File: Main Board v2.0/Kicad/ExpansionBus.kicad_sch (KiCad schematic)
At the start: 0 parts

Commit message: update
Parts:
- added C24, C25, C26, C27, C28: 100n, symbol Device:C
- added J1: Bus_ISA_16bit, Connector_PCBEdge:BUS_AT, symbol Connector:Bus_ISA_16bit
- added U13, U14, U15: 74HC245, symbol 74xx:74HC245
- added U17, U18: 74HC646, symbol My-74-Logic:74HC646
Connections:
- new net +12V: J1.9 (+12V)
- new net +5V: C24.1, C25.1, C26.1, C27.1, C28.1, J1.29 (VCC), J1.3 (+5V), J1.78 (+5V), U13.20 (VCC), U14.20 (VCC), U15.20 (VCC), U17.24 (VCC), U18.24 (VCC)
- new net -12V: J1.7 (-12V)
- new net -5V: J1.5 (-5V)
- new net A0: U13.2 (A0)
- new net A1: U13.3 (A1)
- new net A10: U14.4 (A2)
- new net A11: U14.5 (A3)
- new net A12: U14.6 (A4)
- new net A2: U13.4 (A2)
- new net A3: U13.5 (A3)
- new net A4: U13.6 (A4)
- new net A5: U13.7 (A5)
- new net A6: U13.8 (A6)
- new net A7: U13.9 (A7)
- new net A8: U14.2 (A0)
- new net A9: U14.3 (A1)
- new net BA0: J1.62 (BA00), U13.18 (B0)
- new net BA1: J1.61 (BA01), U13.17 (B1)
- new net BA10: J1.52 (BA10), U14.16 (B2)
- new net BA11: J1.51 (BA11), U14.15 (B3)
- new net BA12: J1.50 (BA12), U14.14 (B4)
- new net BA13: J1.49 (BA13), U14.13 (B5)
- new net BA14: J1.48 (BA14), U14.12 (B6)
- new net BA15: J1.47 (BA15), U14.11 (B7)
- new net BA16: J1.46 (BA16), U15.18 (B0)
- new net BA17: J1.45 (BA17), J1.88 (LA17), U15.17 (B1)
- new net BA18: J1.44 (BA18), J1.87 (LA18), U15.16 (B2)
- new net BA19: J1.43 (BA19), J1.86 (LA19), U15.15 (B3)
- new net BA2: J1.60 (BA02), U13.16 (B2)
- new net BA3: J1.59 (BA03), U13.15 (B3)
- new net BA4: J1.58 (BA04), U13.14 (B4)
- new net BA5: J1.57 (BA05), U13.13 (B5)
- new net BA6: J1.56 (BA06), U13.12 (B6)
- new net BA7: J1.55 (BA07), U13.11 (B7)
- new net BA8: J1.54 (BA08), U14.18 (B0)
- new net BA9: J1.53 (BA09), U14.17 (B1)
- new net BAEN: J1.42 (AEN)
- new net BALE: J1.28 (ALE)
- new net BA_CE: U13.19 (CE), U14.19 (CE), U15.19 (CE)
- new net BA_DIR: U13.1 (A->B), U14.1 (A->B), U15.1 (A->B)
- new net BBUS_REQ: J1.79 (MASTER)
- new net BCLK: J1.20 (CLK)
- new net BD0: J1.40 (DB0), U18.20 (B0)
- new net BD1: J1.39 (DB1), U18.19 (B1)
- new net BD10: J1.93 (D10), U17.18 (B2)
- new net BD11: J1.94 (D11), U17.17 (B3)
- new net BD12: J1.95 (D12), U17.16 (B4)
- new net BD13: J1.96 (D13), U17.15 (B5)
- new net BD14: J1.97 (D14), U17.14 (B6)
- new net BD15: J1.98 (D15), U17.13 (B7)
- new net BD2: J1.38 (DB2), U18.18 (B2)
- new net BD3: J1.37 (DB3), U18.17 (B3)
- new net BD4: J1.36 (DB4), U18.16 (B4)
- new net BD5: J1.35 (DB5), U18.15 (B5)
- new net BD6: J1.34 (DB6), U18.14 (B6)
- new net BD7: J1.33 (DB7), U18.13 (B7)
- new net BD8: J1.91 (D8), U17.20 (B0)
- new net BD8_D16: J1.81 (SBHE)
- new net BD9: J1.92 (D9), U17.19 (B1)
- new net BDMA_END: J1.27 (TC)
- new net BD_DIR: U17.3 (DIR), U18.3 (DIR)
- new net BIO: J1.32 (IO)
- new net BIO_RDY: J1.41 (IO_READY)
- new net BIRQ10: J1.65 (IRQ10)
- new net BIRQ11: J1.66 (IRQ11)
- new net BIRQ12: J1.67 (IRQ12)
- new net BIRQ14: J1.69 (IRQ14)
- new net BIRQ15: J1.68 (IRQ15)
- new net BIRQ2: J1.4 (IRQ2)
- new net BIRQ3: J1.25 (IRQ3)
- new net BIRQ4: J1.24 (IRQ4)
- new net BIRQ5: J1.23 (IRQ5)
- new net BIRQ6: J1.22 (IRQ6)
- new net BIRQ7: J1.21 (IRQ7)
- new net BLA20: J1.85 (LA20), U15.14 (B4)
- new net BLA21: J1.84 (LA21), U15.13 (B5)
- new net BLA22: J1.83 (LA22), U15.12 (B6)
- new net BLA23: J1.82 (LA23), U15.11 (B7)
- new net CLK20: J1.30 (OSC)
- new net D0: U17.4 (A0), U18.4 (A0)
- new net D1: U17.5 (A1), U18.5 (A1)
- new net D2: U17.6 (A2), U18.6 (A2)
- new net D3: U17.7 (A3), U18.7 (A3)
- new net D4: U17.8 (A4), U18.8 (A4)
- new net D5: U17.9 (A5), U18.9 (A5)
- new net D6: U17.10 (A6), U18.10 (A6)
- new net D7: U17.11 (A7), U18.11 (A7)
- new net GND: C24.2, C25.2, C26.2, C27.2, C28.2, J1.1 (GND), J1.10 (GND), J1.31 (GND), J1.80 (GND), U13.10 (GND), U14.10 (GND), U15.10 (GND), U17.12 (GND), U18.12 (GND)
- new net MA13: U14.7 (A5)
- new net MA14: U14.8 (A6)
- new net MA15: U14.9 (A7)
- new net MA16: U15.2 (A0)
- new net MA17: U15.3 (A1)
- new net MA18: U15.4 (A2)
- new net MA19: U15.5 (A3)
- new net MA20: U15.6 (A4)
- new net MA21: U15.7 (A5)
- new net MA22: U15.8 (A6)
- new net MA23: U15.9 (A7)
- new net RESET: J1.2 (RESET)
- new net what?: J1.8 (UNUSED)
- new net ~{B16_IO_CS}: J1.64 (~{IOCS16})
- new net ~{B16_MEM_CS}: J1.63 (~{MEMCS16})
- new net ~{B16_MEM_RD}: J1.89 (~{MEMR})
- new net ~{B16_MEM_WR}: J1.90 (~{MEMW})
- new net ~{B8_MEM_RD}: J1.12 (~{SMEMR})
- new net ~{B8_MEM_WR}: J1.11 (~{SMEMW})
- new net ~{BIO_RD}: J1.14 (~{IOR})
- new net ~{BIO_WR}: J1.13 (~{IOW})
- new net ~{RFSH}: J1.19 (~{REFRESH})
- no-connect marks 0 -> 1
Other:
- note added: "DMA is implemented in the DMA module (ISA card)."
- title: (none) -> Expansion Bus (ISA16)

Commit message: schematic done*
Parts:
- removed C24, C25, C26, C27, C28: 100n, symbol Device:C
- removed U13, U14, U15: 74HC245, symbol 74xx:74HC245
- removed U17, U18: 74HC646, symbol My-74-Logic:74HC646
- added J2: Unused Bus Signals, Connector_PinSocket_2.54mm:PinSocket_2x20_P2.54mm_Vertical, symbol Connector_Generic:Conn_02x20_Row_Letter_First
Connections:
- net BA0 is gone; now on net A0: J1.62 (BA00)
- net BA10 is gone; now on net A10: J1.52 (BA10)
- net BA11 is gone; now on net A11: J1.51 (BA11)
- net BA12 is gone; now on net A12: J1.50 (BA12)
- net BA13 is gone; now on net MA13: J1.49 (BA13)
- net BA14 is gone; now on net MA14: J1.48 (BA14)
- net BA15 is gone; now on net MA15: J1.47 (BA15)
- net BA16 is gone; now on net MA16: J1.46 (BA16)
- net BA2 is gone; now on net A2: J1.60 (BA02)
- net BA3 is gone; now on net A3: J1.59 (BA03)
- net BA4 is gone; now on net A4: J1.58 (BA04)
- net BA5 is gone; now on net A5: J1.57 (BA05)
- net BA6 is gone; now on net A6: J1.56 (BA06)
- net BA7 is gone; now on net A7: J1.55 (BA07)
- net BA8 is gone; now on net A8: J1.54 (BA08)
- net BA9 is gone; now on net A9: J1.53 (BA09)
- net BD0 is gone; now on net D0: J1.40 (DB0)
- net BD1 is gone; now on net D1: J1.39 (DB1)
- net BD2 is gone; now on net D2: J1.38 (DB2)
- net BIO is gone; now on net BA1: J1.32 (IO)
- net BIRQ10 is gone; now on net BD3: J1.65 (IRQ10)
- net BIRQ11 is gone; now on net BD4: J1.66 (IRQ11)
- net BIRQ12 is gone; now on net BD5: J1.67 (IRQ12)
- net BIRQ14 is gone; now on net BD7: J1.69 (IRQ14)
- net BIRQ15 is gone; now on net BD6: J1.68 (IRQ15)
- net BLA20 is gone; now on net MA20: J1.85 (LA20)
- net BLA21 is gone; now on net MA21: J1.84 (LA21)
- net BLA22 is gone; now on net MA22: J1.83 (LA22)
- net BLA23 is gone; now on net MA23: J1.82 (LA23)
- net +5V: now also J2.a19 (Pin_a19)
- net A1: now also J1.61 (BA01)
- net BA1: now also J2.a1 (Pin_a1); no longer J1.61 (BA01)
- net BD10: now also J1.72 (~{DACK5}), J2.b14 (Pin_b14); no longer J1.93 (D10)
- net BD11: now also J1.73 (DRQ5), J2.b15 (Pin_b15); no longer J1.94 (D11)
- net BD12: now also J1.74 (~{DACK6}), J2.b16 (Pin_b16); no longer J1.95 (D12)
- net BD13: now also J1.75 (DRQ6), J2.b17 (Pin_b17); no longer J1.96 (D13)
- net BD14: now also J1.76 (~{DACK7}), J2.b18 (Pin_b18); no longer J1.97 (D14)
- net BD15: now also J1.77 (DRQ7), J2.b19 (Pin_b19); no longer J1.98 (D15)
- net BD3: now also J2.b7 (Pin_b7); no longer J1.37 (DB3)
- net BD4: now also J2.b8 (Pin_b8); no longer J1.36 (DB4)
- net BD5: now also J2.b9 (Pin_b9); no longer J1.35 (DB5)
- net BD6: now also J2.b10 (Pin_b10); no longer J1.34 (DB6)
- net BD7: now also J2.b11 (Pin_b11); no longer J1.33 (DB7)
- net BD8: now also J1.70 (~{DACK0}), J2.b12 (Pin_b12); no longer J1.91 (D8)
- net BD9: now also J1.71 (DRQ0), J2.b13 (Pin_b13); no longer J1.92 (D9)
- net D3: now also J1.37 (DB3)
- net D4: now also J1.36 (DB4)
- net D5: now also J1.35 (DB5)
- net D6: now also J1.34 (DB6)
- net D7: now also J1.33 (DB7)
- net GND: now also J2.a18 (Pin_a18), J2.a20 (Pin_a20)
- net MA17: now also J1.45 (BA17)
- net MA18: now also J1.44 (BA18)
- net MA19: now also J1.43 (BA19)
- net MA24: now also J1.88 (LA17)
- net MA25: now also J1.87 (LA18)
- net BB15: now reaches J1.15 (~{DACK3})
- net BB15: now also J2.b2 (Pin_b2)
- net BB16: now reaches J1.16 (DRQ3)
- net BB16: now also J2.b3 (Pin_b3)
- net ~{CPU_BUSACK}: now reaches J1.17 (~{DACK1})
- net ~{CPU_BUSRQ}: now reaches J1.18 (DRQ1)
- net BB26: now reaches J1.26 (~{DACK2})
- net BB26: now also J2.b4 (Pin_b4)
- net BB6: now reaches J1.6 (DRQ2)
- net BB6: now also J2.b1 (Pin_b1)
- removed net BA17: J1.45 (BA17), J1.88 (LA17)
- removed net BA18: J1.44 (BA18), J1.87 (LA18)
- net BA19 renamed BC6
- net BC6: now also J2.a3 (Pin_a3); no longer J1.43 (BA19)
- net BAEN renamed ~{CPU_M1}
- net BALE renamed BB28
- net BB28: now also J2.b6 (Pin_b6)
- net BBUS_REQ renamed BD17
- net BD17: now also J2.b20 (Pin_b20)
- net BD8_D16 renamed BC1
- net BC1: now also J2.a2 (Pin_a2)
- net BDMA_END renamed BB27
- net BB27: now also J2.b5 (Pin_b5)
- net BIO_RDY renamed ~{CPU_WAIT}
- net RESET renamed ~{CPU_RST}
- net what?: no longer names the net of J1.8 (UNUSED)
- net ~{B16_IO_CS} renamed ~{CPU_IORQ}
- net ~{B16_MEM_CS} renamed ~{CPU_MREQ}
- net ~{B16_MEM_RD} renamed ~{CPU_RD}
- net ~{B16_MEM_WR} renamed ~{CPU_WR}
- net ~{RFSH} renamed ~{CPU_RFSH}
- new net BC11: J1.91 (D8), J2.a4 (Pin_a4)
- new net BC12: J1.92 (D9), J2.a5 (Pin_a5)
- new net BC13: J1.93 (D10), J2.a6 (Pin_a6)
- new net BC14: J1.94 (D11), J2.a7 (Pin_a7)
- new net BC15: J1.95 (D12), J2.a8 (Pin_a8)
- new net BC16: J1.96 (D13), J2.a9 (Pin_a9)
- new net BC17: J1.97 (D14), J2.a10 (Pin_a10)
- new net BC18: J1.98 (D15), J2.a11 (Pin_a11)
- no-connect marks 1 -> 7
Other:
- note added: "10MHz"
- note added: "20MHz"
- note added: "Side A"
- note added: "Side B"
- note removed: "DMA is implemented in the DMA module (ISA card)."
- moved on the sheet: J1

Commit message: board update
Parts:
- removed J2: Unused Bus Signals, Connector_PinSocket_2.54mm:PinSocket_2x20_P2.54mm_Vertical, symbol Connector_Generic:Conn_02x20_Row_Letter_First
- added J2: Conn_02x20_Odd_Even, Connector_PinSocket_2.54mm:PinSocket_2x20_P2.54mm_Vertical, symbol Connector_Generic:Conn_02x20_Odd_Even
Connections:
- net BA1: now also J2.2 (Pin_2)
- net BB15: now also J2.3 (Pin_3)
- net BB16: now also J2.5 (Pin_5)
- net BB26: now also J2.7 (Pin_7)
- net BB27: now also J2.9 (Pin_9)
- net BB28: now also J2.11 (Pin_11)
- net BB6: now also J2.1 (Pin_1)
- net BC1: now also J2.4 (Pin_4)
- net BC11: now also J2.8 (Pin_8)
- net BC12: now also J2.10 (Pin_10)
- net BC13: now also J2.12 (Pin_12)
- net BC14: now also J2.14 (Pin_14)
- net BC15: now also J2.16 (Pin_16)
- net BC16: now also J2.18 (Pin_18)
- net BC17: now also J2.20 (Pin_20)
- net BC18: now also J2.22 (Pin_22)
- net BC6: now also J2.6 (Pin_6)
- net BD10: now also J2.27 (Pin_27)
- net BD11: now also J2.29 (Pin_29)
- net BD12: now also J2.31 (Pin_31)
- net BD13: now also J2.33 (Pin_33)
- net BD14: now also J2.35 (Pin_35)
- net BD15: now also J2.37 (Pin_37)
- net BD17: now also J2.39 (Pin_39)
- net BD3: now also J2.13 (Pin_13)
- net BD4: now also J2.15 (Pin_15)
- net BD5: now also J2.17 (Pin_17)
- net BD6: now also J2.19 (Pin_19)
- net BD7: now also J2.21 (Pin_21)
- net BD8: now also J2.23 (Pin_23)
- net BD9: now also J2.25 (Pin_25)
- net ~{BIACK}: now reaches J1.8 (UNUSED)
- no-connect marks 7 -> 0

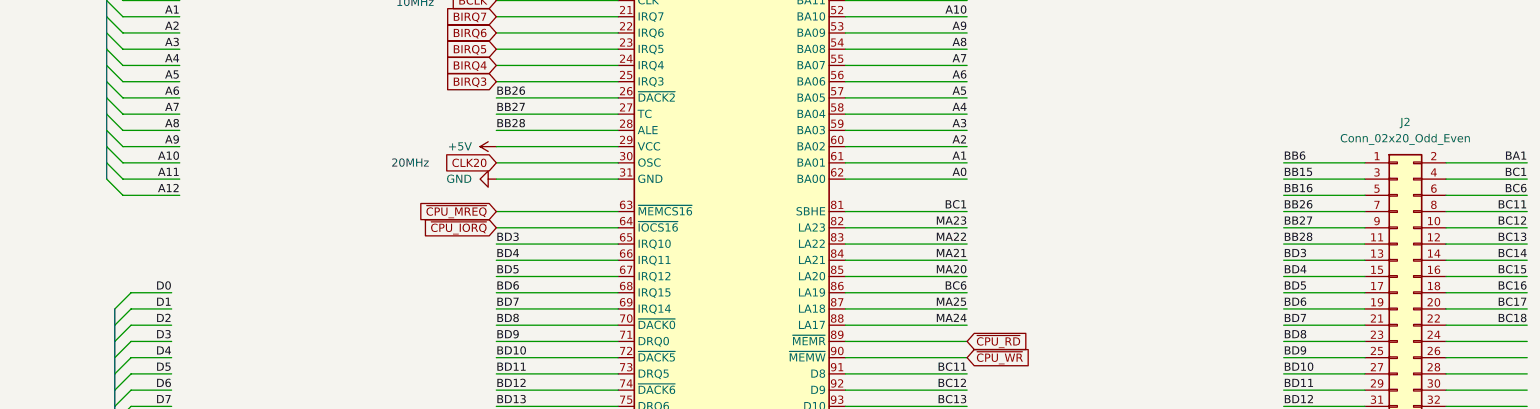
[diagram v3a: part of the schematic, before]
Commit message: schematic update
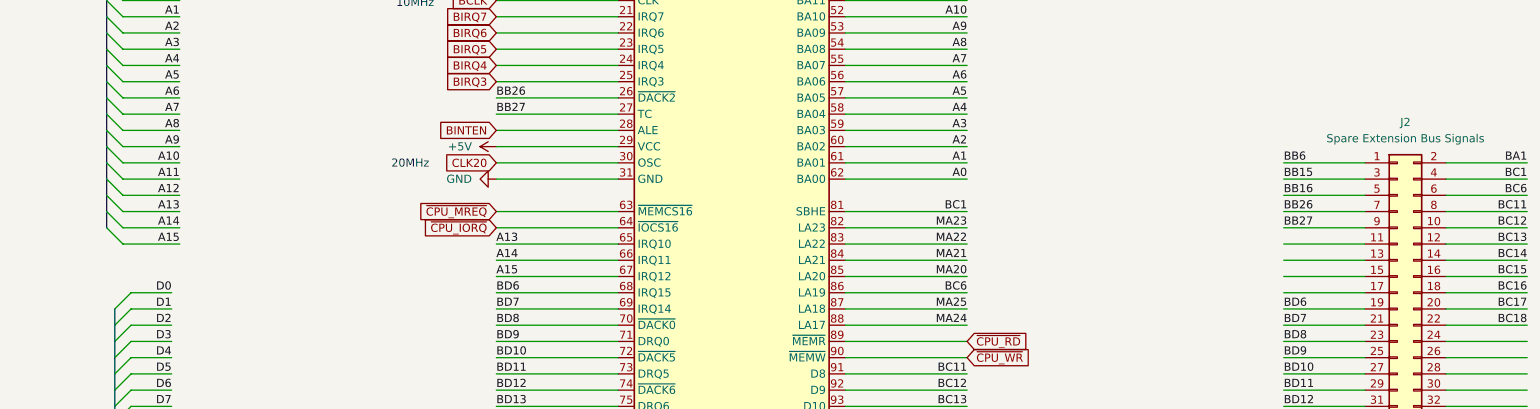
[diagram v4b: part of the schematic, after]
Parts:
- J2: value Conn_02x20_Odd_Even -> Spare Extension Bus Signals
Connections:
- net BB28: no longer names the net of J2.11 (Pin_11)
- net BB28: no longer J1.28 (ALE)
- net BD3: no longer names the net of J2.13 (Pin_13)
- net BD3: no longer J1.65 (IRQ10)
- net BD4: no longer names the net of J2.15 (Pin_15)
- net BD4: no longer J1.66 (IRQ11)
- net BD5: no longer names the net of J2.17 (Pin_17)
- net BD5: no longer J1.67 (IRQ12)
- new net A13: J1.65 (IRQ10)
- new net A14: J1.66 (IRQ11)
- new net A15: J1.67 (IRQ12)
- new net BINTEN: J1.28 (ALE)
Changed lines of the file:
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@@
 	)
 	(bus_entry
+		(at 25.4 110.49)
+		(size 2.54 2.54)
+		(stroke
+			(width 0)
+			(type default)
+		)
+	)
+	(bus_entry
+		(at 25.4 105.41)
+		(size 2.54 2.54)
+		(stroke
+			(width 0)
+			(type default)
+		)
+	)
+	(bus_entry
 		(at 25.4 87.63)
 		(size 2.54 2.54)
@@
 	)
 	(bus_entry
+		(at 25.4 107.95)
+		(size 2.54 2.54)
+		(stroke
+			(width 0)
+			(type default)
+		)
+	)
+	(bus_entry
 		(at 25.4 100.33)
 		(size 2.54 2.54)
@@
 		)
 	)
+	(bus
+		(pts
+			(xy 25.4 102.87) (xy 25.4 110.49)
+		)
+		(stroke
+			(width 0)
+			(type default)
+		)
+	)
 	(wire
 		(pts
@@
 		)
 	)
+	(wire
+		(pts
+			(xy 27.94 107.95) (xy 36.83 107.95)
+		)
+		(stroke
+			(width 0)
+			(type default)
+		)
+	)
 	(bus
 		(pts
@@
 	(wire
 		(pts
+			(xy 27.94 110.49) (xy 36.83 110.49)
+		)
+		(stroke
+			(width 0)
+			(type default)
+		)
+	)
+	(wire
+		(pts
 			(xy 86.36 110.49) (xy 105.41 110.49)
 		)
@@
 	(wire
 		(pts
+			(xy 27.94 113.03) (xy 36.83 113.03)
+		)
+		(stroke
+			(width 0)
+			(type default)
+		)
+	)
+	(wire
+		(pts
 			(xy 140.97 115.57) (xy 160.02 115.57)
 		)
@@
 		)
 	)
-	(label "BD3"
+	(label "A13"
 		(at 86.36 113.03 0)
 		(effects
@@
 		)
 	)
+	(label "A13"
+		(at 36.83 107.95 180)
+		(effects
+			(font
+				(size 1.27 1.27)
+			)
+			(justify right bottom)
+		)
+	)
 	(label "BD6"
 		(at 86.36 120.65 0)
@@
 		)
 	)
+	(label "A15"
+		(at 36.83 113.03 180)
+		(effects
+			(font
+				(size 1.27 1.27)
+			)
+			(justify right bottom)
+		)
+	)
 	(label "MA21"
 		(at 160.02 115.57 180)
@@
 		)
 	)
-	(label "BB28"
-		(at 86.36 95.25 0)
-		(effects
-			(font
-				(size 1.27 1.27)
-			)
-			(justify left bottom)
-		)
-	)
 	(label "MA21"
 		(at 44.45 41.91 180)
@@
 		)
 	)
-	(label "BD3"
-		(at 209.55 115.57 0)
-		(effects
-			(font
-				(size 1.27 1.27)
-			)
-			(justify left bottom)
-		)
-	)
 	(label "MA16"
 		(at 160.02 62.23 180)
@@
 		)
 	)
-	(label "BD4"
+	(label "A14"
 		(at 86.36 115.57 0)
 		(effects
@@
 		)
 	)
+	(label "A14"
+		(at 36.83 110.49 180)
+		(effects
+			(font
+				(size 1.27 1.27)
+			)
+			(justify right bottom)
+		)
+	)
 	(label "BD6"
 		(at 209.55 123.19 0)
@@
 		)
 	)
-	(label "BD4"
-		(at 209.55 118.11 0)
-		(effects
-			(font
-				(size 1.27 1.27)
-			)
-			(justify left bottom)
-		)
-	)
 	(label "A5"
 		(at 36.83 87.63 180)
@@
 		)
 	)
-	(label "BD5"
+	(label "A15"
 		(at 86.36 118.11 0)
 		(effects
@@
 		)
 	)
-	(label "BB28"
-		(at 209.55 113.03 0)
-		(effects
-			(font
-				(size 1.27 1.27)
-			)
-			(justify left bottom)
-		)
-	)
 	(label "BA1"
 		(at 160.02 26.67 180)
@@
 		)
 	)
-	(label "BD5"
-		(at 209.55 120.65 0)
-		(effects
-			(font
-				(size 1.27 1.27)
-			)
-			(justify left bottom)
-		)
-	)
 	(label "BD11"
 		(at 209.55 135.89 0)
@@
 		)
 	)
+	(global_label "BINTEN"
+		(shape input)
+		(at 86.36 95.25 180)
+		(fields_autoplaced yes)
+		(effects
+			(font
+				(size 1.27 1.27)
+			)
+			(justify right)
+		)
+		(property "Intersheetrefs" "${INTERSHEET_REFS}"
+			(at 76.7224 95.25 0)
+			(hide yes)
+			(show_name no)
+			(do_not_autoplace no)
+			(effects
+				(font
+					(size 1.27 1.27)
+				)
+				(justify right)
+			)
+		)
+	)
 	(global_label "BIRQ7"
 		(shape input)
@@
 			)
 		)
-		(property "Value" "Conn_02x20_Odd_Even"
+		(property "Value" "Spare Extension Bus Signals"
 			(at 228.6 96.52 0)
 			(show_name no)

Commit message: schematic updates
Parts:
- removed J2: Spare Extension Bus Signals, Connector_PinSocket_2.54mm:PinSocket_2x20_P2.54mm_Vertical, symbol Connector_Generic:Conn_02x20_Odd_Even
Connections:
- net BB15 is gone; now on net ~{BIACK}: J1.15 (~{DACK3})
- net BB16 is gone; now on net BINTEN: J1.16 (DRQ3)
- net BB26 is gone; now on net BIRQ2: J1.26 (~{DACK2})
- net BINTEN: no longer J1.28 (ALE)
- net BIRQ2: no longer J1.4 (IRQ2)
- net ~{BIACK}: no longer J1.8 (UNUSED)
- net BB27 renamed BIRQ1
- net BB6: no longer names the net of J1.6 (DRQ2)
- net BD10 renamed BINTACK4
- net BD11 renamed BINTACK5
- net BD12 renamed BINTACK6
- net BD13 renamed BINTACK7
- net BD14: no longer names the net of J1.76 (~{DACK7})
- net BD15: no longer names the net of J1.77 (DRQ7)
- net BD17: no longer names the net of J1.79 (MASTER)
- net BD6 renamed BINTACK0
- net BD7 renamed BINTACK1
- net BD8 renamed BINTACK2
- net BD9 renamed BINTACK3
- new net BB4: J1.4 (IRQ2)
- new net BIRQ0: J1.28 (ALE)
- no-connect marks 0 -> 5
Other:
- note added: "5 bus signals not connected. Can be used for inter-module signals."
- note added: "Side A (Components)"
- note added: "Side B (Solder)"
- note removed: "Side A"
- note removed: "Side B"

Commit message: board
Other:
- note added: "What is the max thickness of PCB that fits into ISA slot? This seems to be 1.6mm."
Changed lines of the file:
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@@
+		)
+	)
+	(text "What is the max thickness of PCB that fits into ISA slot?\nThis seems to be 1.6mm."
+		(exclude_from_sim no)
+		(at 230.632 104.648 0)
+		(effects
+			(font
+				(size 1.27 1.27)
+			)
 		)
 	)
